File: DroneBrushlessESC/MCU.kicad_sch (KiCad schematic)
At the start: 7 parts

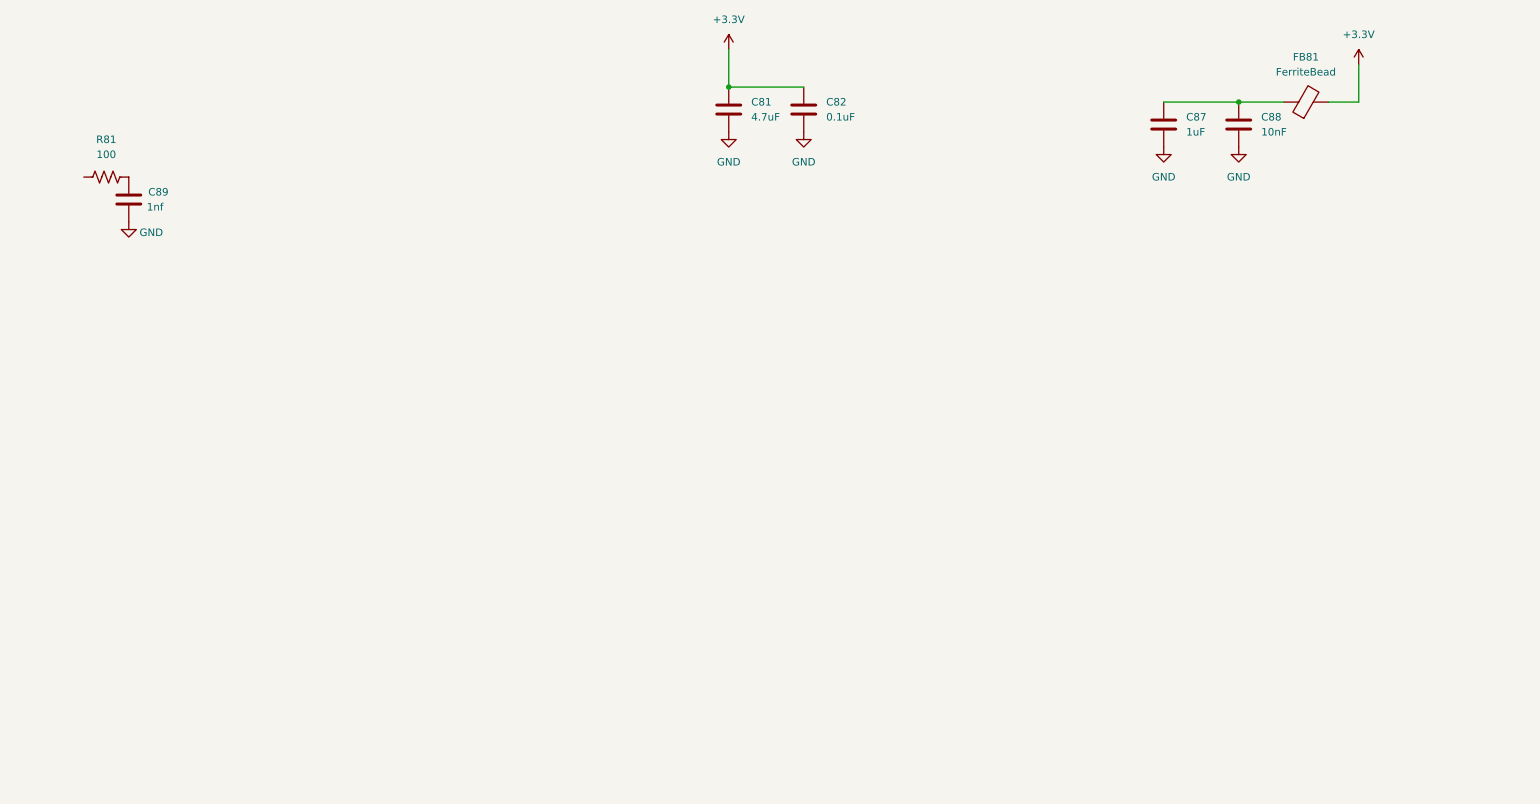
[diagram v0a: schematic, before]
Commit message: Completed schematic for brushless ESC and added needed components to main board.  The plan is to mount the ESCs on the main board using 2.54mm Vert Conn Headers
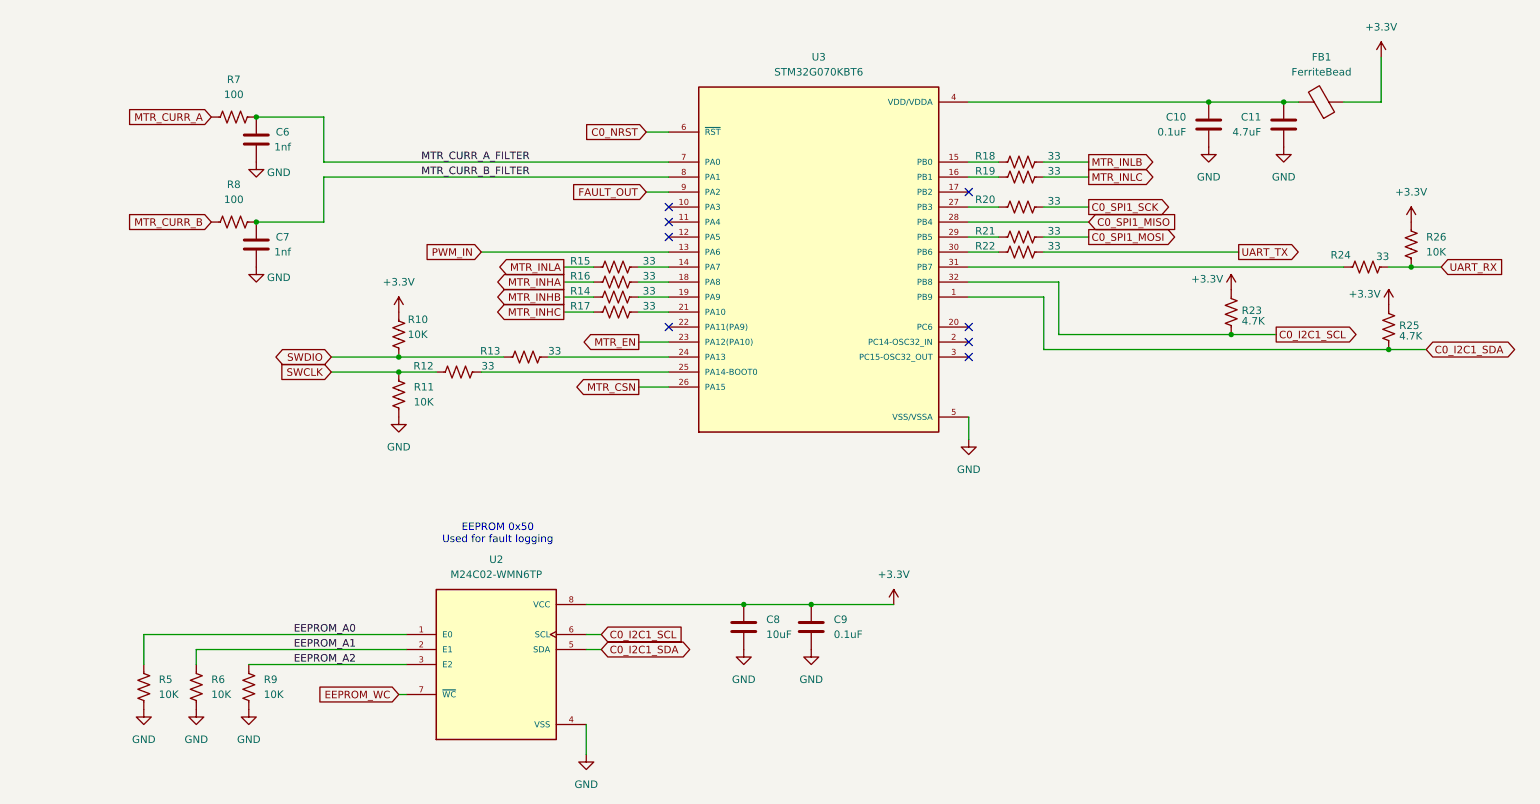
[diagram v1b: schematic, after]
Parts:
- removed C87: 1uF, Capacitor_SMD:C_0402_1005Metric, symbol Device:C
- removed C88: 10nF, Capacitor_SMD:C_0402_1005Metric, symbol Device:C
- removed FB81: FerriteBead, Inductor_SMD:L_0805_2012Metric, symbol Device:FerriteBead
- added C7: 1nf, Capacitor_SMD:C_0402_1005Metric, symbol Device:C
- added C8: 10uF, Capacitor_SMD:C_1206_3216Metric, symbol Device:C
- added C9: 0.1uF, Capacitor_SMD:C_0402_1005Metric, symbol Device:C
- added FB1: FerriteBead, Inductor_SMD:L_0805_2012Metric, symbol Device:FerriteBead
- added R10, R11, R26, R5, R6, R9: 10K, Resistor_SMD:R_0402_1005Metric, symbol Device:R_US
- added R12, R13, R14, R15, R16, R17, R18, R19, R20, R21, R22, R24: 33, Resistor_SMD:R_0402_1005Metric, symbol Device:R_US
- added R23, R25: 4.7K, Resistor_SMD:R_0402_1005Metric, symbol Device:R_US
- added R8: 100, Resistor_SMD:R_0402_1005Metric, symbol Device:R_US
- added U2: M24C02-WMN6TP, Library:SOIC127P600X175-8N, symbol Global:M24C02-WMN6TP
- added U3: STM32G070KBT6, Library:QFP80P900X900X160-32N, symbol Global:STM32G070KBT6
- renumbered C82 to C10, C81 to C11, C89 to C6, R81 to R7
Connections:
- net +3.3V: now also C8.1, C9.1, FB1.1, R10.2, R23.2, R25.2, R26.2, U2.8 (VCC); no longer C10.1, C11.1
- net GND: now also C7.2, C8.2, C9.2, R11.1, R5.1, R6.1, R9.1, U2.4 (VSS), U3.5 (VSS/VSSA)
- net MTR_CURR_A: now reaches R7.1
- net MTR_CURR_A_FILTER: now reaches C6.1, R7.2
- net MTR_CURR_A_FILTER: now also U3.7 (PA0)
- new net: C10.1, C11.1, FB1.2, U3.4 (VDD/VDDA)
- new net: R24.1, U3.31 (PB7)
- new net: R19.1, U3.16 (PB1)
- new net: R17.2, U3.21 (PA10)
- new net: R21.1, U3.29 (PB5)
- new net: R15.2, U3.14 (PA7)
- new net: R16.2, U3.18 (PA8)
- new net: R18.1, U3.15 (PB0)
- new net: R14.2, U3.19 (PA9)
- new net: R13.2, U3.24 (PA13)
- new net: R12.2, U3.25 (PA14-BOOT0)
- new net: R20.1, U3.27 (PB3)
- new net: R22.1, U3.30 (PB6)
- new net C0_I2C1_SCL: R23.1, U2.6 (SCL), U3.32 (PB8)
- new net C0_I2C1_SDA: R25.1, U2.5 (SDA), U3.1 (PB9)
- new net C0_NRST: U3.6 (~{RST})
- new net C0_SPI1_MISO: U3.28 (PB4)
- new net C0_SPI1_MOSI: R21.2
- new net C0_SPI1_SCK: R20.2
- new net EEPROM_A0: R5.2, U2.1 (E0)
- new net EEPROM_A1: R6.2, U2.2 (E1)
- new net EEPROM_A2: R9.2, U2.3 (E2)
- new net EEPROM_WC: U2.7 (~{WC})
- new net FAULT_OUT: U3.9 (PA2)
- new net MTR_CSN: U3.26 (PA15)
- new net MTR_CURR_B: R8.1
- new net MTR_CURR_B_FILTER: C7.1, R8.2, U3.8 (PA1)
- new net MTR_EN: U3.23 (PA12(PA10))
- new net MTR_INHA: R16.1
- new net MTR_INHB: R14.1
- new net MTR_INHC: R17.1
- new net MTR_INLA: R15.1
- new net MTR_INLB: R18.2
- new net MTR_INLC: R19.2
- new net PWM_IN: U3.13 (PA6)
- new net SWCLK: R11.2, R12.1
- new net SWDIO: R10.1, R13.1
- new net UART_RX: R24.2, R26.1
- new net UART_TX: R22.2
- no-connect marks 0 -> 8
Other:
- note added: "EEPROM 0x50 Used for fault logging"
- moved on the sheet: C10, C11, C6, R7

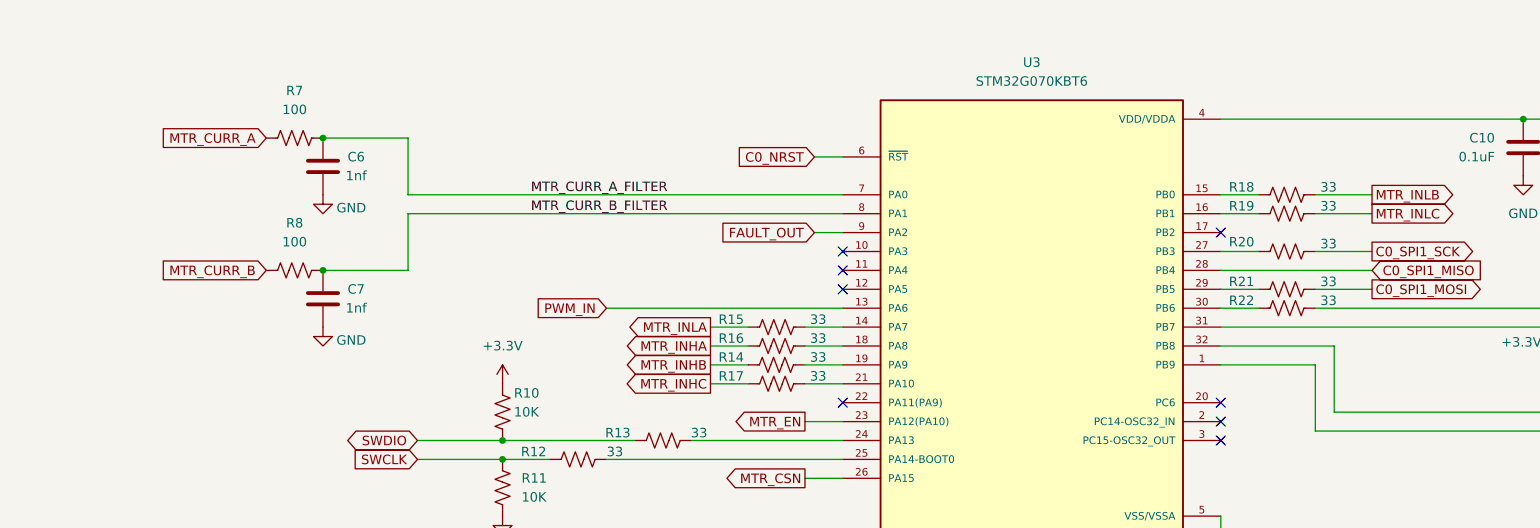
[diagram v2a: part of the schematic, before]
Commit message: Finished brushless driver layout
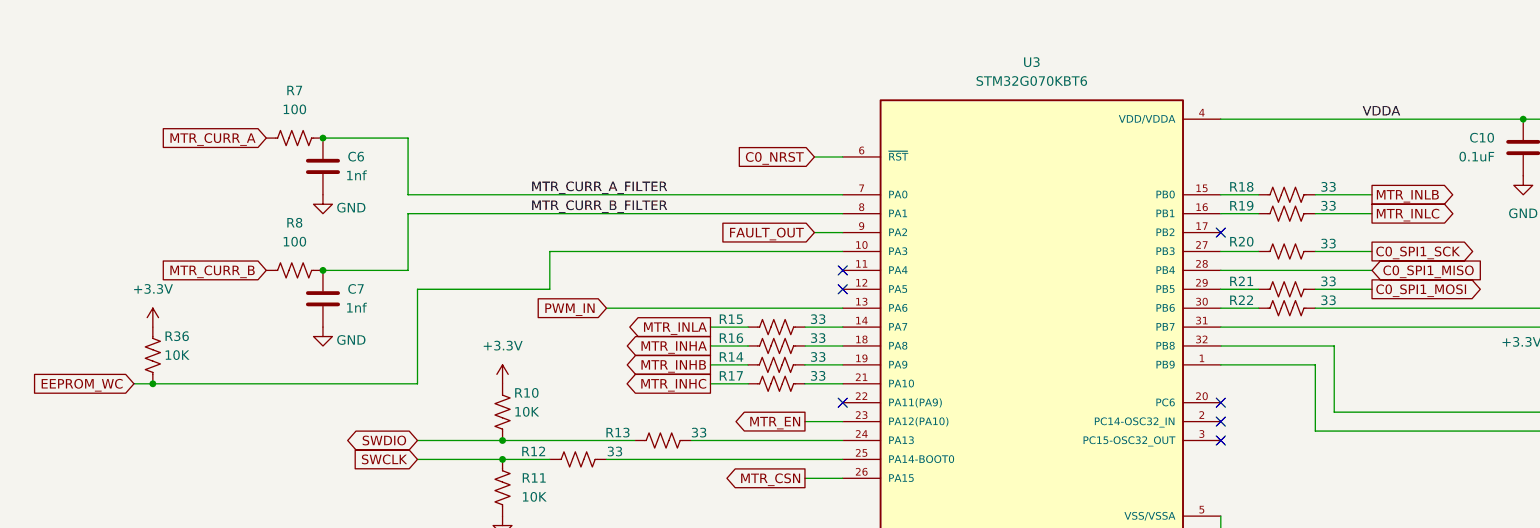
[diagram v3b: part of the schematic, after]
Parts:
- added R36: 10K, Resistor_SMD:R_0402_1005Metric, symbol Device:R_US
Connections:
- net +3.3V: now also R36.2
- net EEPROM_WC: now also U3.10 (PA3), R36.1
- net VDDA: now reaches C10.1, C11.1, FB1.2, U3.4 (VDD/VDDA)
- no-connect marks 8 -> 7
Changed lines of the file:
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@@
 	)
 	(junction
+		(at 33.02 80.01)
+		(diameter 0)
+		(color 0 0 0 0)
+	)
+	(junction
 		(at 229.87 44.45)
 		(diameter 0)
@@
 		(at 125.73 82.55)
 	)
-	(no_connect
-		(at 125.73 62.23)
-	)
 	(wire
 		(pts
@@
 	(wire
 		(pts
+			(xy 33.02 80.01) (xy 68.58 80.01)
+		)
+		(stroke
+			(width 0)
+			(type default)
+		)
+	)
+	(wire
+		(pts
 			(xy 251.46 72.39) (xy 256.54 72.39)
 		)
@@
 	(wire
 		(pts
+			(xy 86.36 62.23) (xy 125.73 62.23)
+		)
+		(stroke
+			(width 0)
+			(type default)
+		)
+	)
+	(wire
+		(pts
 			(xy 229.87 44.45) (xy 217.17 44.45)
 		)
@@
 	(wire
 		(pts
+			(xy 68.58 67.31) (xy 86.36 67.31)
+		)
+		(stroke
+			(width 0)
+			(type default)
+		)
+	)
+	(wire
+		(pts
+			(xy 30.48 80.01) (xy 33.02 80.01)
+		)
+		(stroke
+			(width 0)
+			(type default)
+		)
+	)
+	(wire
+		(pts
 			(xy 54.61 139.7) (xy 81.28 139.7)
 		)
@@
 	(wire
 		(pts
+			(xy 68.58 80.01) (xy 68.58 67.31)
+		)
+		(stroke
+			(width 0)
+			(type default)
+		)
+	)
+	(wire
+		(pts
 			(xy 176.53 72.39) (xy 240.03 72.39)
 		)
@@
 	(wire
 		(pts
+			(xy 86.36 67.31) (xy 86.36 62.23)
+		)
+		(stroke
+			(width 0)
+			(type default)
+		)
+	)
+	(wire
+		(pts
 			(xy 191.77 74.93) (xy 176.53 74.93)
 		)
@@
 		)
 	)
+	(label "VDDA"
+		(at 195.58 44.45 0)
+		(effects
+			(font
+				(size 1.27 1.27)
+			)
+			(justify left bottom)
+		)
+	)
 	(global_label "C0_I2C1_SCL"
 		(shape output)
@@
 		)
 	)
+	(global_label "EEPROM_WC"
+		(shape input)
+		(at 30.48 80.01 180)
+		(fields_autoplaced yes)
+		(effects
+			(font
+				(size 1.27 1.27)
+			)
+			(justify right)
+		)
+		(property "Intersheetrefs" "${INTERSHEET_REFS}"
+			(at 16.1859 80.01 0)
+			(effects
+				(font
+					(size 1.27 1.27)
+				)
+				(justify right)
+			)
+		)
+	)
 	(global_label "C0_SPI1_SCK"
 		(shape output)
@@
 	)
 	(symbol
+		(lib_id "power:+3.3V")
+		(at 33.02 72.39 0)
+		(unit 1)
+		(exclude_from_sim no)
+		(in_bom yes)
+		(on_board yes)
+		(dnp no)
+		(fields_autoplaced yes)
+		(property "Reference" "#PWR01"
+			(at 33.02 76.2 0)
+			(effects
+				(font
+					(size 1.27 1.27)
+				)
+				(hide yes)
+			)
+		)
+		(property "Value" "+3.3V"
+			(at 33.02 67.31 0)
+			(effects
+				(font
+					(size 1.27 1.27)
+				)
+			)
+		)
+		(property "Footprint" ""
+			(at 33.02 72.39 0)
+			(effects
+				(font
+					(size 1.27 1.27)
+				)
+				(hide yes)
+			)
+		)
+		(property "Datasheet" ""
+			(at 33.02 72.39 0)
+			(effects
+				(font
+					(size 1.27 1.27)
+				)
+				(hide yes)
+			)
+		)
+		(property "Description" "Power symbol creates a global label with name \"+3.3V\""
+			(at 33.02 72.39 0)
+			(effects
+				(font
+					(size 1.27 1.27)
+				)
+				(hide yes)
+			)
+		)
+		(pin "1"
+		)
+		(instances
+			(project "DroneBrushlessESC"
+				(path "/3aa1a426-ad7e-4dd6-a1c5-7f97b630afc0/b8819b5d-6d92-40b6-816c-12e04bd43e9a"
+					(reference "#PWR01")
+					(unit 1)
+				)
+			)
+		)
+	)
+	(symbol
 		(lib_id "Device:R_US")
 		(at 220.98 80.01 180)
@@
 					(unit 1)
 				)
+			)
+		)
+	)
+	(symbol
+		(lib_id "Device:R_US")
+		(at 33.02 76.2 180)
+		(unit 1)
+		(exclude_from_sim no)
+		(in_bom yes)
+		(on_board yes)
+		(dnp no)
+		(property "Reference" "R36"
+			(at 34.544 73.66 0)
+			(effects
+				(font
+					(size 1.27 1.27)
+				)
+				(justify right)
+			)
+		)
+		(property "Value" "10K"
+			(at 34.544 76.2 0)
+			(effects
+				(font
+					(size 1.27 1.27)
+				)
+				(justify right)
+			)
+		)
+		(property "Footprint" "Resistor_SMD:R_0402_1005Metric"
+			(at 32.004 75.946 90)
+			(effects
+				(font
+					(size 1.27 1.27)
+				)
+				(hide yes)
+			)
+		)
+		(property "Datasheet" "~"
+			(at 33.02 76.2 0)
+			(effects
+				(font
+					(size 1.27 1.27)
+				)
+				(hide yes)
+			)
+		)
+		(property "Description" "Resistor, US symbol"
+			(at 33.02 76.2 0)
+			(effects
+				(font
+					(size 1.27 1.27)
+				)
+				(hide yes)
+			)
+		)
+		(pin "1"
+		)
+		(pin "2"
+		)
+		(instances
+			(project "DroneBrushlessESC"
+				(path "/3aa1a426-ad7e-4dd6-a1c5-7f97b630afc0/b8819b5d-6d92-40b6-816c-12e04bd43e9a"
+					(reference "R36")
+					(unit 1)
+				)

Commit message: Finished Schematic for controller
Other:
- title: (none) -> MCU
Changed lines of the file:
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@@
 	(generator_version "9.0")
 	(paper "A4")
+	(title_block
+		(title "MCU")
+		(date "2026-02-23")
+		(rev "0-1")
+	)
 	(text "EEPROM 0x50\nUsed for fault logging"
 		(exclude_from_sim no)
